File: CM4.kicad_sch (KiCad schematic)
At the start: 5 parts, among them J1 Conn_02x05_Odd_Even, J2 HDMI_A_2.0, U1 RaspberryPi-CM4Lite

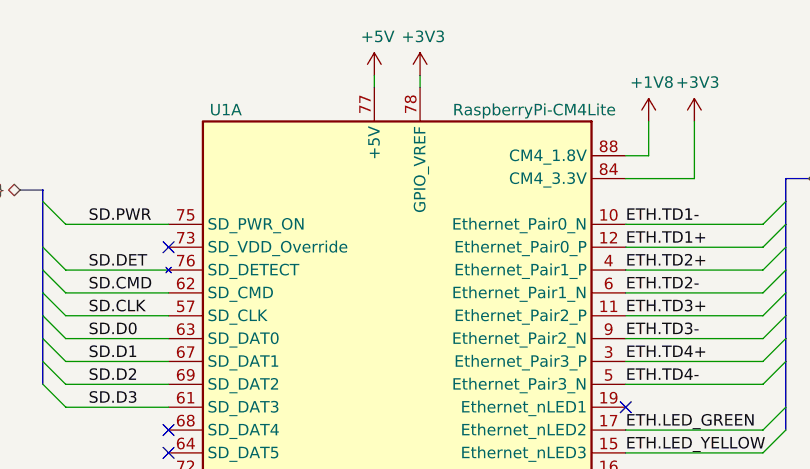
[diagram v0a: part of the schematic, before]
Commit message: PCB[WIP]/SCH:
changes:
-more routing
-added poe negotiation disabled when +12V is present on the DC jack
-modified m.2 "holes"

Signed-off-by: Dominik Sliwa <dominik@sliwa.io>
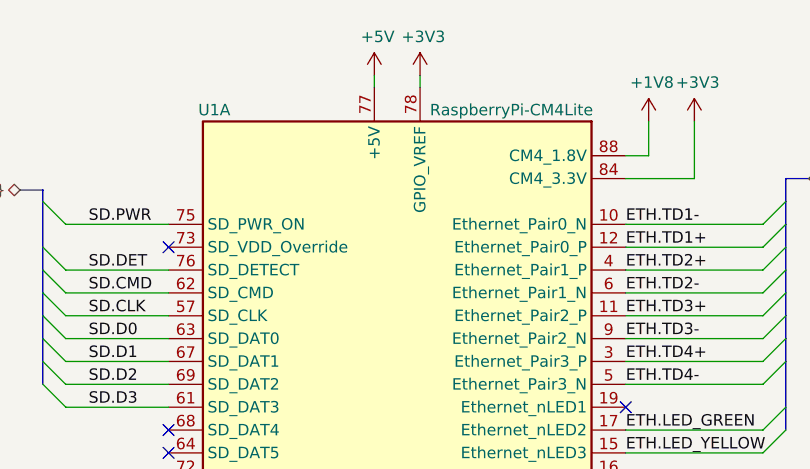
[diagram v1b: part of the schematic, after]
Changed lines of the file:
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@@
   (symbol (lib_id "LightBlue:RaspberryPi-CM4Lite") (at 63.5 88.9 0) (unit 1)
     (in_bom yes) (on_board yes)
-    (property "Reference" "U1" (id 0) (at 44.45 30.48 0))
-    (property "Value" "RaspberryPi-CM4Lite" (id 1) (at 78.74 30.48 0))
+    (property "Reference" "U1" (id 0) (at 43.18 30.48 0))
+    (property "Value" "RaspberryPi-CM4Lite" (id 1) (at 76.2 30.48 0))
     (property "Footprint" "LightBlue:RaspberryPi-CM4" (id 2) (at 76.2 147.32 0)
       (effects (font (size 1.27 1.27)) hide)
     )
-    (property "Datasheet" "" (id 3) (at 63.5 88.9 0)
+    (property "Datasheet" "https://datasheets.raspberrypi.org/cm4/cm4-datasheet.pdf" (id 3) (at 63.5 88.9 0)
       (effects (font (size 1.27 1.27)) hide)
     )

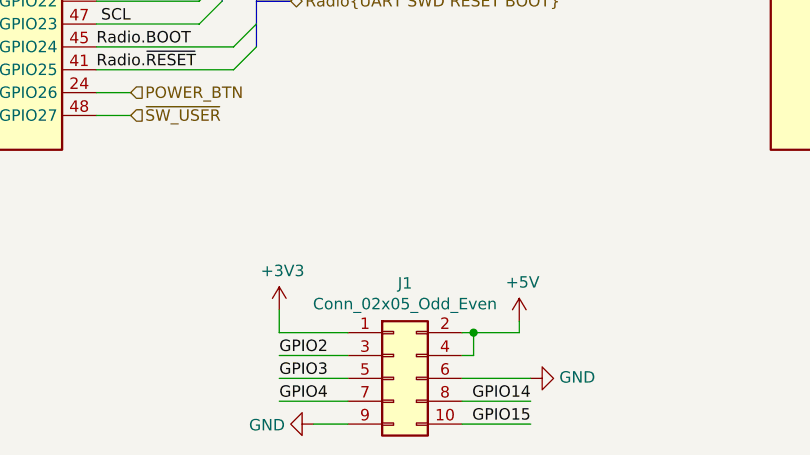
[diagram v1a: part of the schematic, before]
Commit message: Change connector reference designators
Make them ordered logically, based importance and placement on the
board.

Signed-off-by: Stefan Agner <stefan@agner.ch>
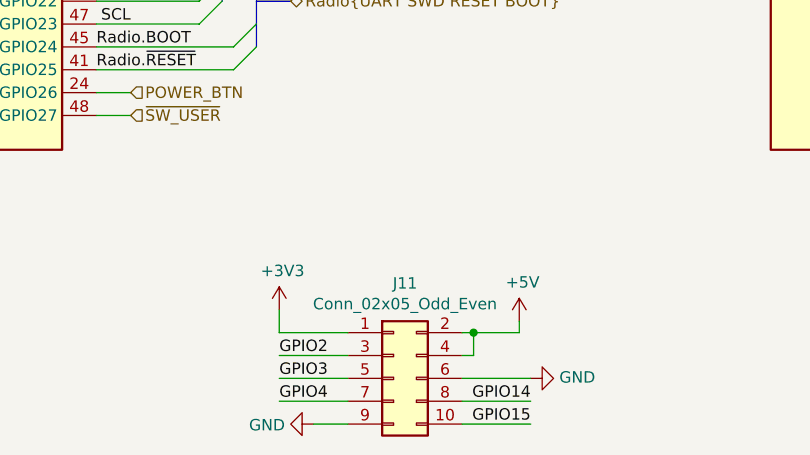
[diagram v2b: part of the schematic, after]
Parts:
- renumbered J1 to J11
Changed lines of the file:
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@@
   (symbol (lib_id "Connector_Generic:Conn_02x05_Odd_Even") (at 121.92 171.45 0) (unit 1)
     (in_bom yes) (on_board yes)
-    (property "Reference" "J1" (id 0) (at 123.19 160.8898 0))
+    (property "Reference" "J11" (id 0) (at 123.19 160.8898 0))
     (property "Value" "Conn_02x05_Odd_Even" (id 1) (at 123.19 163.1885 0))
     (property "Footprint" "Connector_PinHeader_2.54mm:PinHeader_2x05_P2.54mm_Vertical" (id 2) (at 121.92 171.45 0)

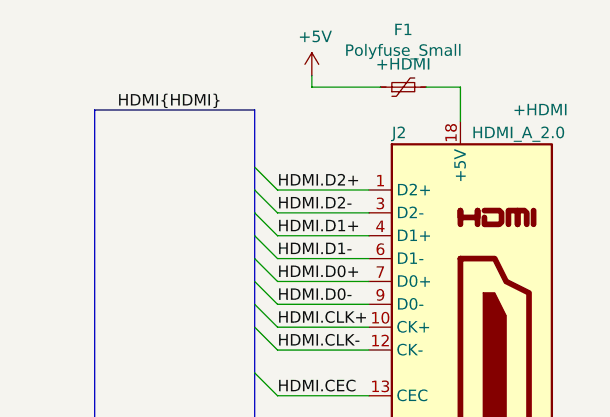
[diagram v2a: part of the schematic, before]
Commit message: Improve SW and D (LED) ordering and silkscreen
Make sure switches (SW) are ordered logically. Also use D1 through D6
for LEDs.

Signed-off-by: Stefan Agner <stefan@agner.ch>
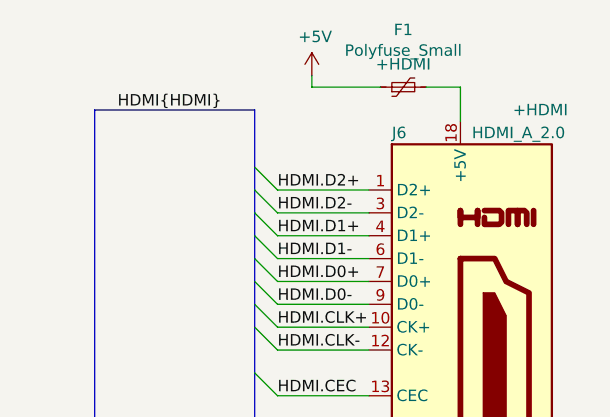
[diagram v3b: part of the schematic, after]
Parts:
- renumbered J2 to J6
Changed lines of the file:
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@@
     (comment 2 "Light Blue")
   )
+  (bus_alias "HDMI" (members "D0+" "D0-" "D1+" "D1-" "D2+" "D2-" "CLK+" "CLK-" "CEC" "HPD" "SDA" "SCL"))
+  (bus_alias "UART" (members "TXD" "RXD" "CTS" "RTS"))
+  (bus_alias "SD" (members "D[0..3]" "CMD" "CLK" "PWR" "DET"))
   (bus_alias "PCIe" (members "~RST" "~CLKREQ" "CLK+" "CLK-" "TX+" "TX-" "RX+" "RX-"))
-  (bus_alias "SD" (members "D[0..3]" "CMD" "CLK" "PWR" "DET"))
-  (bus_alias "UART" (members "TXD" "RXD" "CTS" "RTS"))
-  (bus_alias "HDMI" (members "D0+" "D0-" "D1+" "D1-" "D2+" "D2-" "CLK+" "CLK-" "CEC" "HPD" "SDA" "SCL"))
   (junction (at 130.81 166.37) (diameter 0.9144) (color 0 0 0 0))
   (junction (at 260.35 90.17) (diameter 1.016) (color 0 0 0 0))
@@
   (symbol (lib_id "Connector:HDMI_A_1.4") (at 265.43 59.69 0) (unit 1)
     (in_bom yes) (on_board yes)
-    (property "Reference" "J2" (id 0) (at 257.81 33.02 0)
+    (property "Reference" "J6" (id 0) (at 257.81 33.02 0)
       (effects (font (size 1.27 1.27)) (justify left))
     )

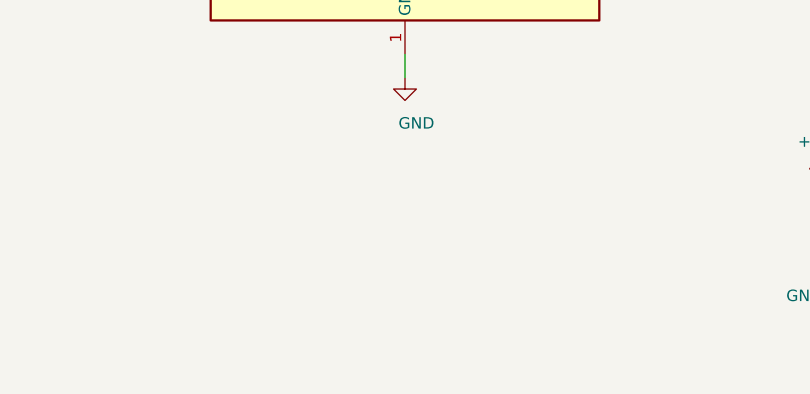
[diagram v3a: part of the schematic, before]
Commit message: Add CM4 board to board connectors
Add the CM4 board to board connectors using separate symbols. This is a
bit a hack, but makes sure two pieces appear in the BOM.

Also, this seems to upgrade all the schematic to the latest KiCad
schematic version.

Signed-off-by: Stefan Agner <stefan@agner.ch>
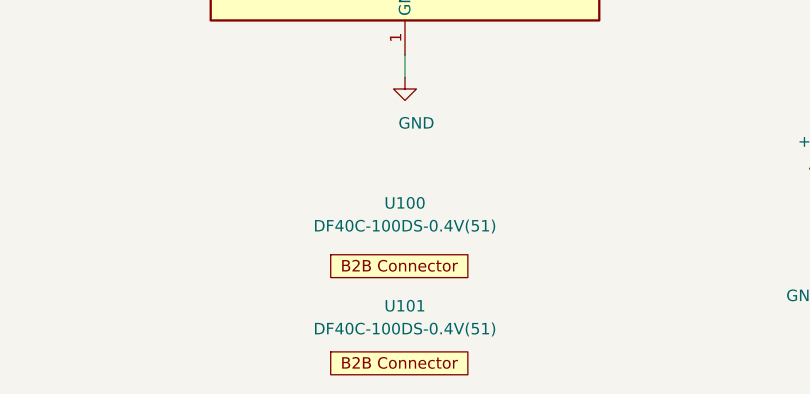
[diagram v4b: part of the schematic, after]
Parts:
- added U100, U101: DF40C-100DS-0.4V(51), symbol LightBlue:DF40C-100DS-0.4V(51)

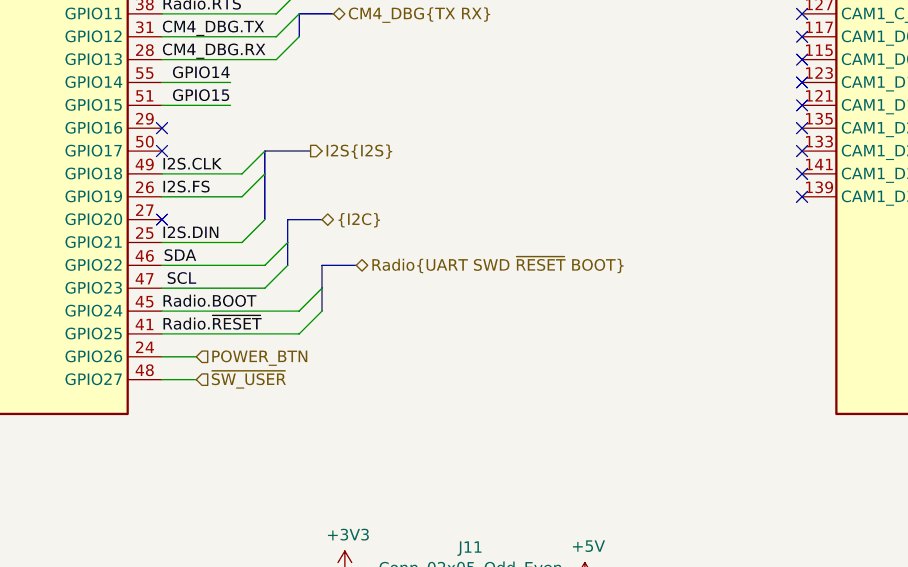
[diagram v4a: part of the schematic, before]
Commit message: Add pull-ups for Radio.~RESET/~BOOT
Make sure those signals are well defined even when not be driven from
the CM4 side. Also rename Radio.BOOT to Radio.~BOOT since its a low
active signal.

Fixes: #10

Signed-off-by: Stefan Agner <stefan@agner.ch>
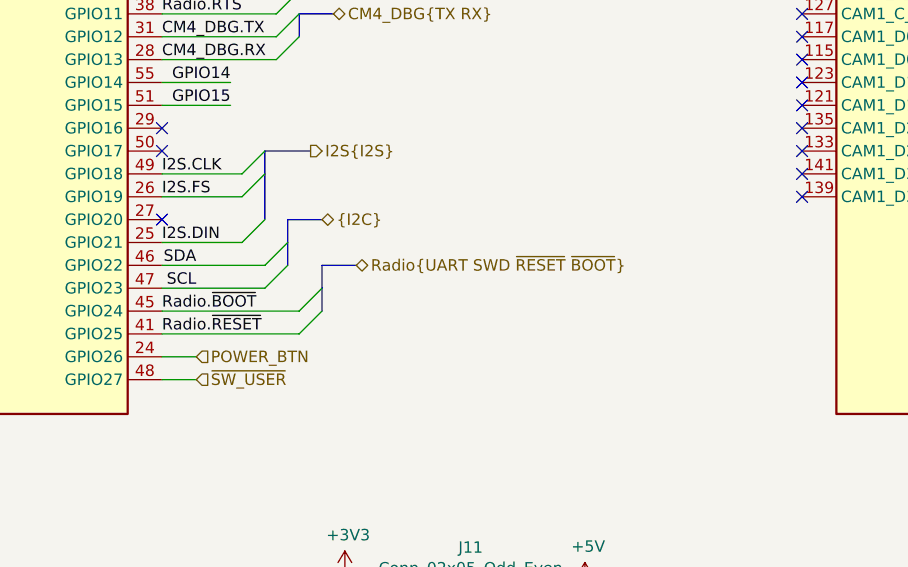
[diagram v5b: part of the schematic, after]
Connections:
- net Radio.BOOT renamed Radio.~BOOT
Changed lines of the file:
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@@
     (comment 2 "Light Blue")
   )
+  (bus_alias "HDMI" (members "D0+" "D0-" "D1+" "D1-" "D2+" "D2-" "CLK+" "CLK-" "CEC" "HPD" "SDA" "SCL"))
+  (bus_alias "UART" (members "TXD" "RXD" "CTS" "RTS"))
+  (bus_alias "SD" (members "D[0..3]" "CMD" "CLK" "PWR" "DET"))
   (bus_alias "PCIe" (members "~RST" "~CLKREQ" "CLK+" "CLK-" "TX+" "TX-" "RX+" "RX-"))
-  (bus_alias "SD" (members "D[0..3]" "CMD" "CLK" "PWR" "DET"))
-  (bus_alias "UART" (members "TXD" "RXD" "CTS" "RTS"))
-  (bus_alias "HDMI" (members "D0+" "D0-" "D1+" "D1-" "D2+" "D2-" "CLK+" "CLK-" "CEC" "HPD" "SDA" "SCL"))
   (junction (at 130.81 166.37) (diameter 0.9144) (color 0 0 0 0))
   (junction (at 260.35 90.17) (diameter 1.016) (color 0 0 0 0))
@@
     (effects (font (size 1.27 1.27)) (justify left bottom))
   )
-  (label "Radio.BOOT" (at 88.9 134.62 0)
+  (label "Radio.~BOOT" (at 88.9 134.62 0)
     (effects (font (size 1.27 1.27)) (justify left bottom))
   )
@@
     (effects (font (size 1.27 1.27)) (justify left))
   )
-  (hierarchical_label "Radio{UART SWD ~RESET BOOT}" (shape bidirectional) (at 110.49 129.54 0)
+  (hierarchical_label "Radio{UART SWD ~RESET ~BOOT}" (shape bidirectional) (at 110.49 129.54 0)
     (effects (font (size 1.27 1.27)) (justify left))
   )

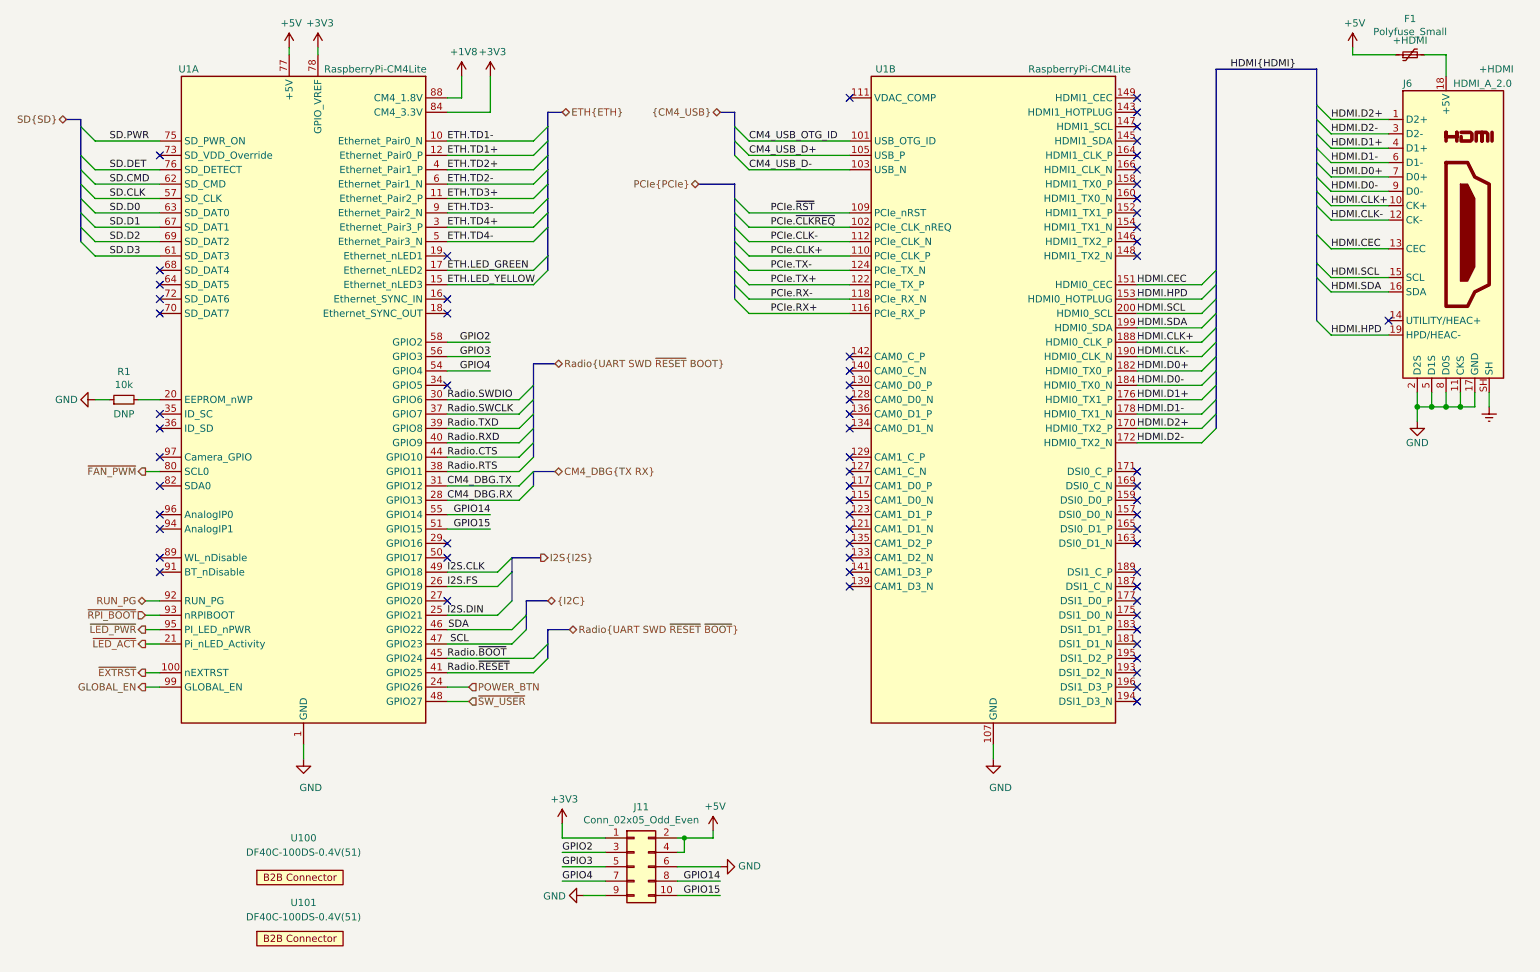
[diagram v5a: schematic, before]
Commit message: Redesign buttons/switches
Remove power/reset/recovery switch. Power and reset is not really required
and recovery mode (USB Boot) can be triggered via jumper. Make the Fan
and RPiLED a new separate config so we can leave them unpopulated. Add a
second GPIO controlled switch.

Fixes: #16

Signed-off-by: Stefan Agner <stefan@agner.ch>
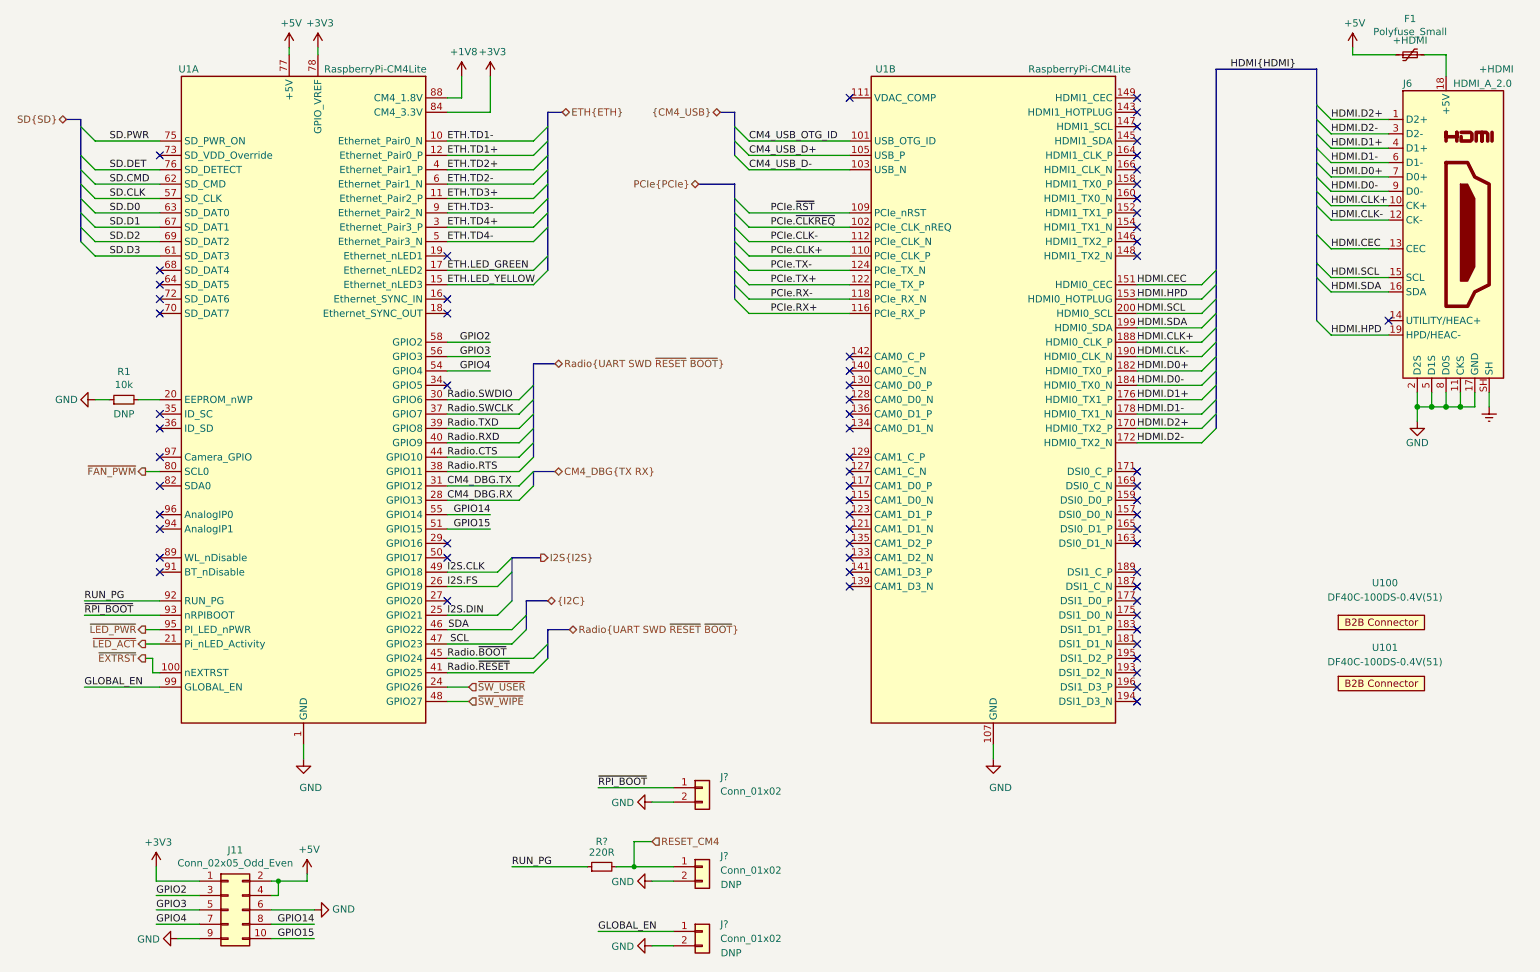
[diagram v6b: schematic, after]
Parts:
- added J? (x3): Conn_01x02, symbol Connector_Generic:Conn_01x02
- added R?: 220R, symbol Device:R_Small
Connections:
- net POWER_BTN is gone; now on net ~SW_USER: U1.24 (GPIO26)
- net GLOBAL_EN: now also J?.1 (Pin_1)
- net GND: now also J?.2 (Pin_2), J?.2 (Pin_2), J?.2 (Pin_2)
- net RUN_PG: now also R?.1
- net ~RPI_BOOT: now also J?.1 (Pin_1)
- net ~SW_USER: no longer U1.48 (GPIO27)
- new net RESET_CM4: J?.1 (Pin_1), R?.2
- new net ~SW_WIPE: U1.48 (GPIO27)
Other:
- moved on the sheet: J11, U100, U101

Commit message: Replace full sized HDMI with micro HDMI
Fixes: #17

Signed-off-by: Stefan Agner <stefan@agner.ch>
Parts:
- J6: footprint LightBlue:HDMI_A_Molex_2086588131_Horizontal -> Connector_HDMI:HDMI_Micro-D_Molex_46765-1x01; PartNumber 208658-8131 -> 0467651301
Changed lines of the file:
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@@
       (effects (font (size 1.27 1.27)) (justify left))
     )
-    (property "Footprint" "LightBlue:HDMI_A_Molex_2086588131_Horizontal" (id 2) (at 266.065 59.69 0)
+    (property "Footprint" "Connector_HDMI:HDMI_Micro-D_Molex_46765-1x01" (id 2) (at 266.065 59.69 0)
       (effects (font (size 1.27 1.27)) hide)
     )
@@
       (effects (font (size 1.27 1.27)) hide)
     )
-    (property "PartNumber" "208658-8131" (id 6) (at 265.43 59.69 0)
+    (property "PartNumber" "0467651301" (id 6) (at 265.43 59.69 0)
       (effects (font (size 1.27 1.27)) hide)
     )
